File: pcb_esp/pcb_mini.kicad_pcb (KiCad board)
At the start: 2 copper layers, 81.3 x 33 mm, 47 parts, among them J1 Conn_01x05_Pin, J2 Conn_01x04_Pin, J3 Conn_02x03_Odd_Even, J4 Conn_01x05_Pin, J5 Conn_01x05_Pin, J6 Conn_01x05_Pin, J7 Conn_01x08_Pin, J8 Conn_02x03_Odd_Even, Q1 DMG2302U, Q2 DMG2301L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

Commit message: pcb_esp: Version 20240902
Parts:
- added C10: 100n, Capacitor_SMD:C_0402_1005Metric, F.Cu at (67.7, 82.6)
- added C7: 100n, Capacitor_SMD:C_0402_1005Metric, F.Cu at (87.4, 65.0)
- added C8: 100n, Capacitor_SMD:C_0402_1005Metric, F.Cu at (85.5, 82.5)
- added Q2: DMG2301L, Package_TO_SOT_SMD:SOT-23, F.Cu at (88.9, 82.5)
- added Q4: DMG2301L, Package_TO_SOT_SMD:SOT-23, F.Cu at (71.1, 82.5)
- added R6: 10k, Resistor_SMD:R_0402_1005Metric, F.Cu at (90.0, 78.9)
- added R8: 10k, Resistor_SMD:R_0402_1005Metric, F.Cu at (71.8, 78.9)
- added TP1: TestPoint_Probe, TestPoint:TestPoint_Loop_D3.80mm_Drill2.8mm, F.Cu at (39.4, 85.1)
- ? (x2), U4: moved to B.Cu
- C1, C2, C4, C5, C6: footprint Capacitor_SMD:C_0402_1005Metric_Pad0.74x0.62mm_HandSolder -> Capacitor_SMD:C_0402_1005Metric
- C11: renamed from C8; footprint Capacitor_SMD:C_0402_1005Metric_Pad0.74x0.62mm_HandSolder -> Capacitor_SMD:C_0402_1005Metric
- C3: footprint Capacitor_SMD:C_0402_1005Metric_Pad0.74x0.62mm_HandSolder -> Capacitor_SMD:C_0402_1005Metric; moved to B.Cu
- C9: renamed from C7; footprint Capacitor_SMD:C_0402_1005Metric_Pad0.74x0.62mm_HandSolder -> Capacitor_SMD:C_0402_1005Metric
- J1: value Conn_01x05_Pin -> Conn_01x06; footprint Connector_PinHeader_2.54mm:PinHeader_1x05_P2.54mm_Vertical -> Connector_PinHeader_2.54mm:PinHeader_1x06_P2.54mm_Vertical
- J2: value Conn_01x04_Pin -> Conn_01x06; footprint Connector_PinHeader_2.54mm:PinHeader_1x04_P2.54mm_Vertical -> Connector_PinHeader_2.54mm:PinHeader_1x06_P2.54mm_Vertical; moved to F.Cu
- R1, R2, R3, R4, R5: footprint Resistor_SMD:R_0402_1005Metric_Pad0.72x0.64mm_HandSolder -> Resistor_SMD:R_0402_1005Metric
- R10: renamed from R8; footprint Resistor_SMD:R_0402_1005Metric_Pad0.72x0.64mm_HandSolder -> Resistor_SMD:R_0402_1005Metric
- R11: renamed from R9; footprint Resistor_SMD:R_0402_1005Metric_Pad0.72x0.64mm_HandSolder -> Resistor_SMD:R_0402_1005Metric
- R12: renamed from R10; footprint Resistor_SMD:R_0402_1005Metric_Pad0.72x0.64mm_HandSolder -> Resistor_SMD:R_0402_1005Metric
- R13: renamed from R11; footprint Resistor_SMD:R_0402_1005Metric_Pad0.72x0.64mm_HandSolder -> Resistor_SMD:R_0402_1005Metric
- R14: renamed from R12; footprint Resistor_SMD:R_0402_1005Metric_Pad0.72x0.64mm_HandSolder -> Resistor_SMD:R_0402_1005Metric
- R15: renamed from R13; footprint Resistor_SMD:R_0402_1005Metric_Pad0.72x0.64mm_HandSolder -> Resistor_SMD:R_0402_1005Metric
- R16: renamed from R14; footprint Resistor_SMD:R_0402_1005Metric_Pad0.72x0.64mm_HandSolder -> Resistor_SMD:R_0402_1005Metric
- R17: renamed from R15; footprint Resistor_SMD:R_0402_1005Metric_Pad0.72x0.64mm_HandSolder -> Resistor_SMD:R_0402_1005Metric
- R18: renamed from R16; footprint Resistor_SMD:R_0402_1005Metric_Pad0.72x0.64mm_HandSolder -> Resistor_SMD:R_0402_1005Metric
- R7: renamed from R6; footprint Resistor_SMD:R_0402_1005Metric_Pad0.72x0.64mm_HandSolder -> Resistor_SMD:R_0402_1005Metric
- R9: renamed from R7; footprint Resistor_SMD:R_0402_1005Metric_Pad0.72x0.64mm_HandSolder -> Resistor_SMD:R_0402_1005Metric
- moved J2 26.8 mm to (73.7, 87.0)
- moved ? 18.8 mm to (52.7, 81.6), turned to 180 degrees (x2)
- moved J1 12.8 mm to (91.4, 87.0), turned to -90 degrees
- moved C3 5.85 mm to (68.2, 62.5), turned to 90 degrees
- moved U4 3.07 mm to (71.0, 62.5), turned to 180 degrees
- moved R14 1.52 mm to (38.6, 70.6)
- moved R15 1.52 mm to (37.1, 70.6)
- moved J7 0.76 mm to (63.5, 57.7)
- renumbered Q2 to Q3, TP1 to TP2, TP2 to TP3
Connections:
- J1 pad 1: +BATT -> /Power/AUX_VBAT
- J1 pad 2: /Power/PA0 -> /Power/AUX_VBAT
- J1 pad 3: /Power/PA1 -> /Power/MOSI
- J1 pad 4: /Power/BTN -> /Power/PA4
- J2 pad 1: +3V3 -> /Power/AUX_3V3
- J2 pad 2: GND -> /Power/AUX_3V3
- J2 pad 3: /Power/PA4 -> /ESP/EPD_DC
- J2 pad 4: /Power/MOSI -> /ESP/SCL
- J8 pad 2: /ESP/RST -> /ESP/GPIO0
- J8 pad 5: /ESP/GPIO0 -> /ESP/RST
- U3 pad 12: /Power/PA1 -> /Power/AUX_EN
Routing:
- net GND: track 8.71 -> 66.9 mm, vias 32 -> 53
- net /Power/AUX_EN: track 0.00 -> 47.8 mm, vias 0 -> 4
- net /Power/MOSI: track 53.5 -> 84.2 mm, vias 2 -> 5
- net /Power/PA4: track 55.6 -> 83.1 mm, vias 3 -> 5
- net /Power/BTN: track 41.9 -> 14.7 mm, vias 4 -> 2
- net /Power/PA1: track 25.8 -> 0.00 mm
- net /Power/PA0: track 28.1 -> 2.90 mm, vias 0 -> 1
- net /ESP/SCL: track 45.8 -> 60.2 mm, vias 2 -> 4
- net /Power/AUX_3V3: track 0.00 -> 11.5 mm
- net /Power/AUX_VBAT: track 0.00 -> 11.5 mm
- net /ESP/EPD_DC: track 55.0 -> 66.1 mm, vias 4 -> 6
- net +3V3: track 79.6 -> 89.7 mm, vias 4 -> 3
- net /ESP/GPIO0: track 40.0 -> 32.4 mm
- net /ESP/RST: track 12.8 -> 19.9 mm
- net +BATT: track 119.9 -> 113.2 mm
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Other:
- board text added: "AVR/ESP dev board zhiyb@20240902"
- board text added: "R RX E G TX 0"
- board text added: "RCI GON"
- board text added: "VC DA CL IT GD"
- board text added: "VC GD TX CK CS DC RS BY"
- board text removed: "AVR/ESP dev board zhiyb@20240828"

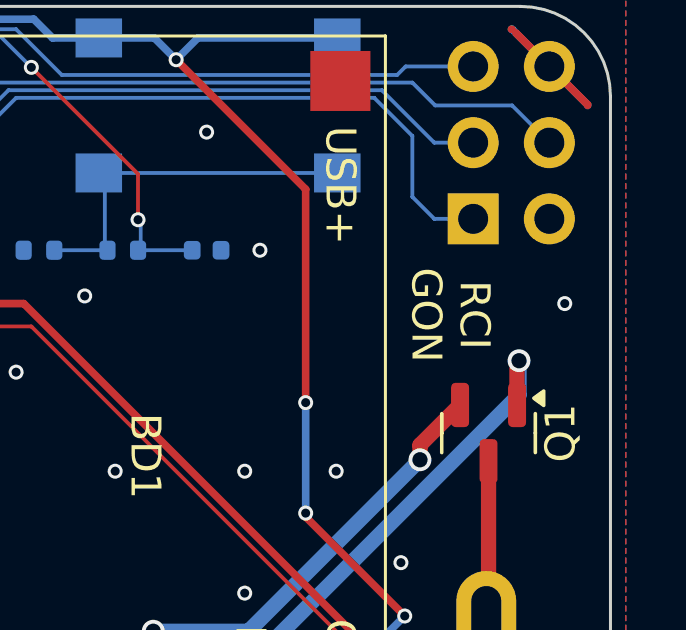
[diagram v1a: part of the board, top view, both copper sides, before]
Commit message: pcb_esp: AVR ISP pinout silkscreen correction
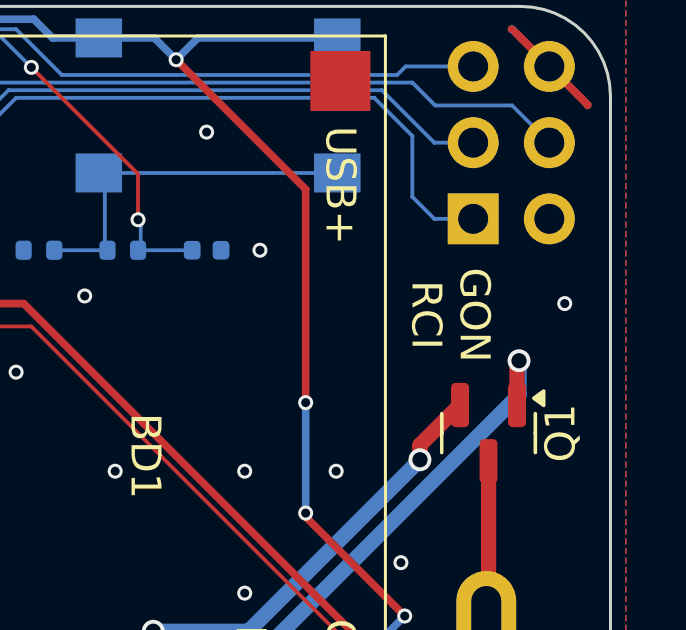
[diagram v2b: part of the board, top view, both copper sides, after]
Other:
- board text added: "GON RCI"
- board text removed: "RCI GON"
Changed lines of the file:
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@@
 		)
 	)
-	(gr_text "RCI \nGON"
-		(at 111.506 66.167 -90)
+	(gr_text "GON\nRCI"
+		(at 111.506 66.167 270)
 		(layer "F.SilkS")
 		(effects
